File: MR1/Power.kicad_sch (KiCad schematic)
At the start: 39 parts, among them J3 USB_C_Receptacle_USB2.0, U1 LM27762, U11 LP5907MFX-1.8, U33 NCP163ASN330T1G, U4 LT3045xDD, U5 LT3094xDD, U7 SN65220

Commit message: Signed-off-by: lokimetasmith <lokimail@gmail.com>
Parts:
- removed C34: 100nF, Capacitor_SMD:C_0402_1005Metric, symbol Device:C
- removed U11: LP5907MFX-1.8, Package_TO_SOT_SMD:SOT-23-5, symbol Regulator_Linear:LP5907MFX-1.8
- added C40, C42: 100u, symbol Device:C_Polarized_Small_US
- added D1, D2: 1N4148WS, Diode_SMD:D_SOD-323, symbol Diode:1N4148WS
- added Q1: BCP53, Package_TO_SOT_SMD:SOT-223-3_TabPin2, symbol Transistor_BJT:BCP53
- added Q2: BCP56, Package_TO_SOT_SMD:SOT-223-3_TabPin2, symbol Transistor_BJT:BCP56
- added R49, R50: 1K, Resistor_SMD:R_0402_1005Metric, symbol Device:R
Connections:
- net +Vp: now also D1.2 (A), Q2.3 (E); no longer C15.2, R24.2, U1.11 (OUT+)
- net -Vp: now also D2.1 (K), Q1.3 (E); no longer C14.1, R18.1, U1.6 (OUT-), U5.1 (IN), U5.13 (IN), U5.2 (IN), U5.3 (EN/UV)
- net GND: now also C14.2, C15.1, C16.2, C18.2, R25.1, R26.2, U1.13 (PAD), U1.4 (GND), C40.2, C42.1
- net GNDA: no longer C14.2, C15.1, C16.2, C18.2, R25.1, R26.2, U1.13 (PAD), U1.4 (GND)
- new net: C42.2, D2.2 (A), Q1.1 (B), R50.2
- new net: C40.1, D1.1 (K), Q2.1 (B), R49.2
- new net: U5.1 (IN), U5.13 (IN), U5.2 (IN), U5.3 (EN/UV)
- new net +Vp_cm: C15.2, Q2.2 (C), Q2.4 (C), R24.2, R49.1, U1.11 (OUT+)
- new net -Vp_cm: C14.1, Q1.2 (C), Q1.4 (C), R18.1, R50.1, U1.6 (OUT-)
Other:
- moved on the sheet: C10, C118, C121, C17, D82, R145, U33

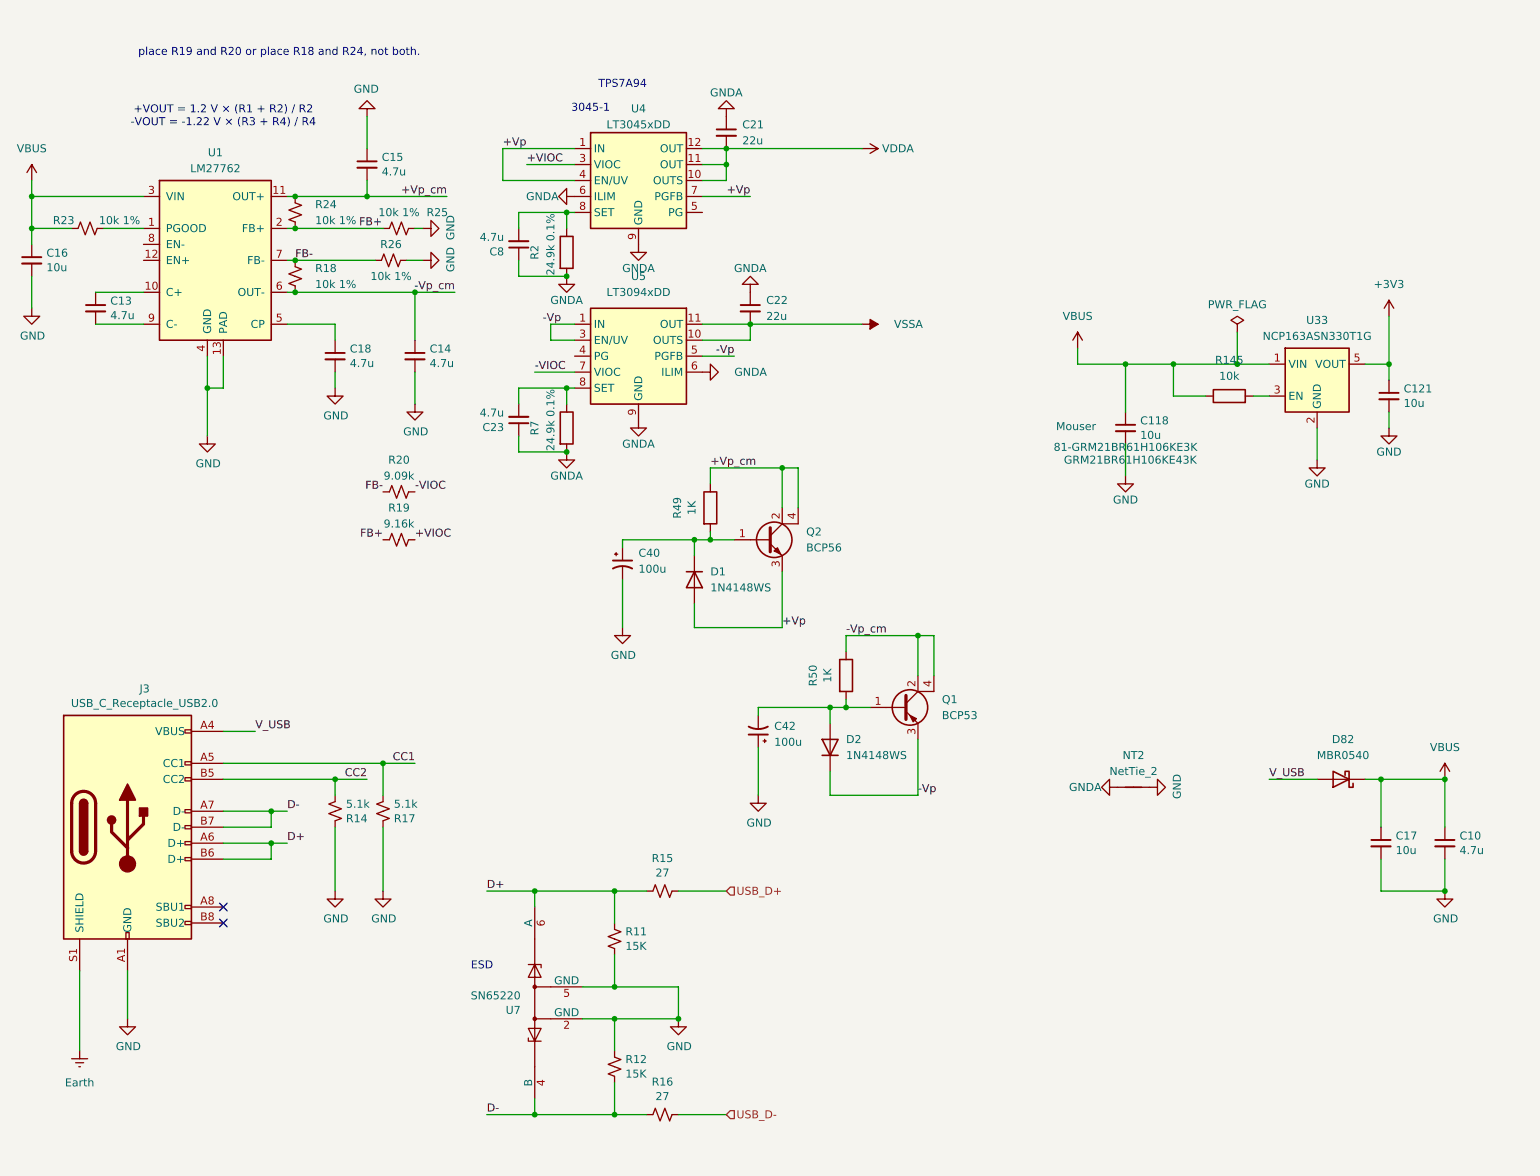
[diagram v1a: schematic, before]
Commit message: feat(cad,firmware,interposer): PTFE interposer, deliverables pipeline, and firmware
- CAD & Interposer:
  - Modeled PTFE_Interposer (55.0 x 51.962 x 0.8 mm) with central wafer diamond cutout
  - Dual-sided silver chloride (Ag/AgCl) ribbon electrode pads (30 deg Cis, 210 deg Trans)
  - 6-pad pogo pin landing array and 4 fluidic pass-throughs with weep duct relief
  - Verified 0 physical collisions across cartridge stack and housings (100% green)
- Deliverables & Export Pipeline:
  - Created automated export system (Makefile, scripts/export_manager.py, scripts/export_all.sh)
  - Full cataloging of 159 deliverables (30 STLs, 13 DXFs, STEPs, Gerbers, WireViz)
  - Added E2E tests (tests/test_exports_e2e.py) and legacy parity tests (tests/test_legacy_feature_parity.py)
- Firmware & Schematics:
  - ESP32-S3 firmware with 100 kHz USB streaming, FreeRTOS dual-core tasks, Web UI
  - Added fast AD40xx SPI driver, MCP4822 DAC driver, leak detection, and pump UART
  - SBU auto-polarity detection and I2C routing in MR1 schematics
- Docs & Environment:
  - Added setup_env.sh, setup_env.ps1, requirements.txt, EXPORTS.md
  - Updated README.md, TODO.md, atlas.project.json, and walkthrough.md
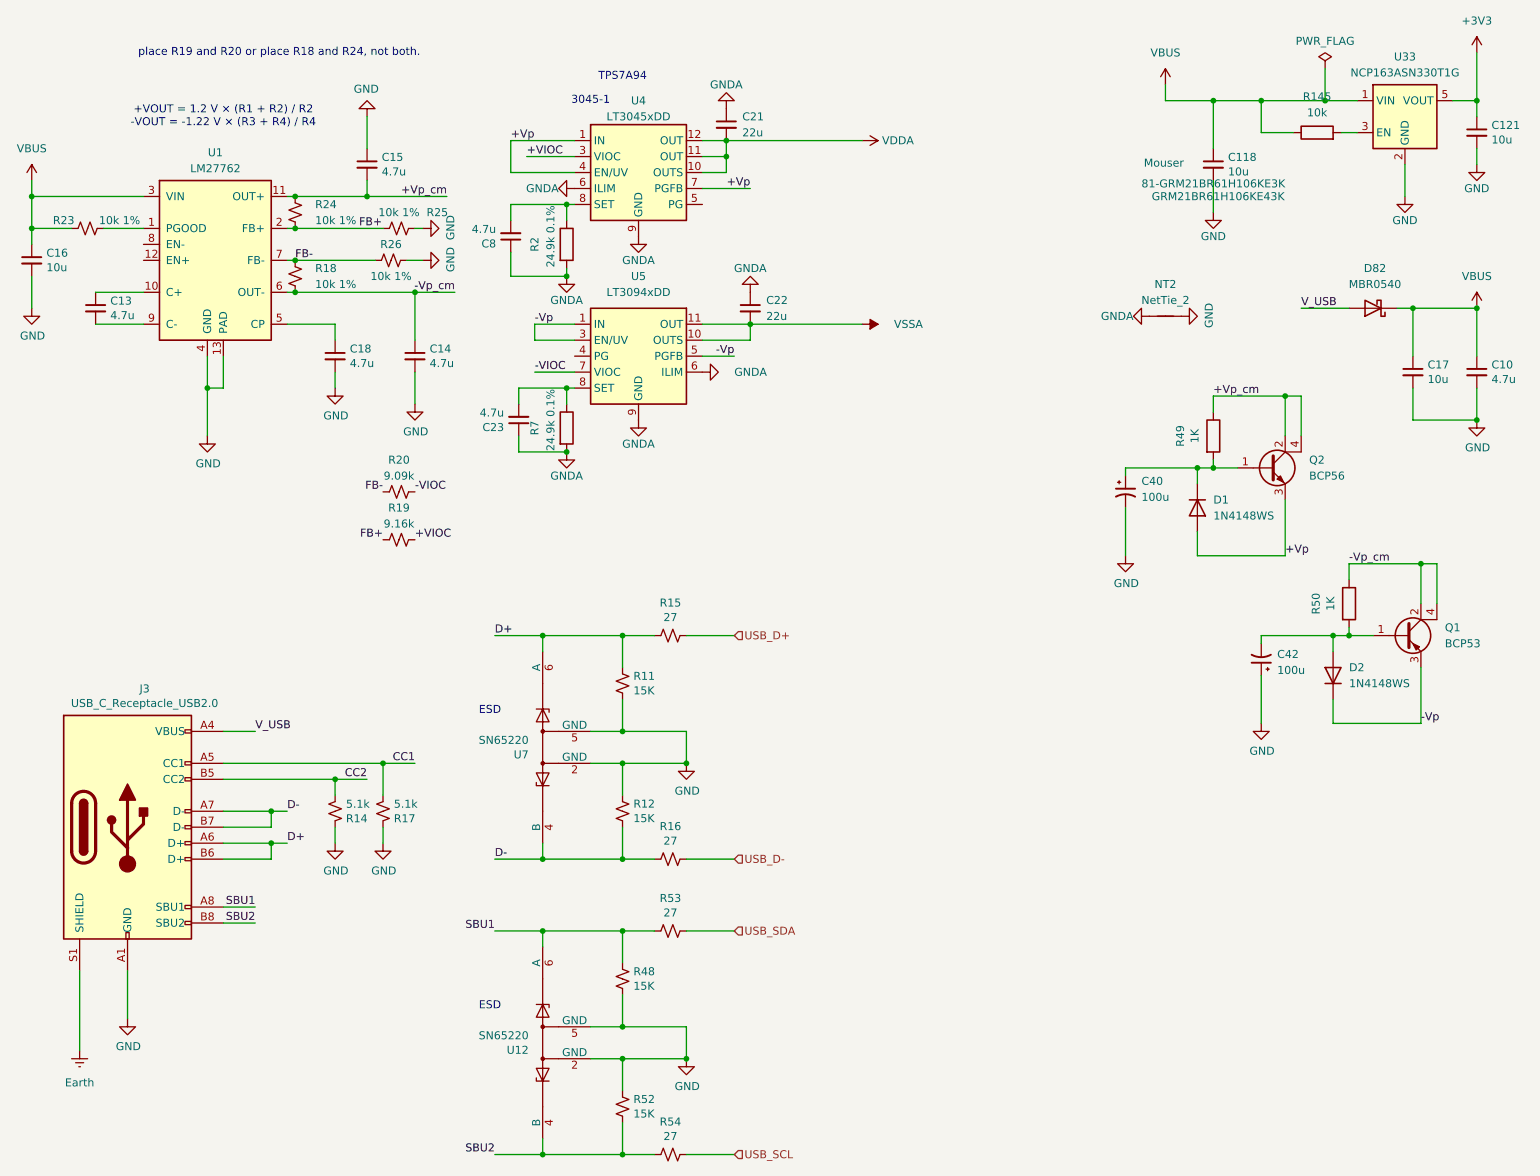
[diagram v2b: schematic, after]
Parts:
- added R48, R52: 15K, Resistor_SMD:R_0402_1005Metric, symbol temp-sensor-rescue:R_Small_US-Device-temp-sensor-rescue
- added R53, R54: 27, Resistor_SMD:R_0402_1005Metric, symbol temp-sensor-rescue:R_Small_US-Device-temp-sensor-rescue
- added U12: SN65220, Package_TO_SOT_SMD:SOT-23-6, symbol twig:SN65220-Power_Protection_passthrough
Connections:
- net -Vp: now also U5.1 (IN), U5.13 (IN), U5.2 (IN), U5.3 (EN/UV)
- net GND: now also R48.2, R52.1, U12.2 (GND), U12.5 (GND)
- net SBU1: now reaches J3.A8 (SBU1)
- net SBU1: now also R48.1, R53.1, U12.1, U12.6 (A)
- net SBU2: now reaches J3.B8 (SBU2)
- net SBU2: now also R52.2, R54.1, U12.3, U12.4 (B)
- new net USB_SCL: R54.2
- new net USB_SDA: R53.2
- no-connect marks 2 -> 0
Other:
- moved on the sheet: C10, C118, C121, C17, C21, C40, C42, C8, D1, D2, D82, NT2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

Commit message: commiting pcb changes
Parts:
- Q1: value BCP53 -> 2SA1037; footprint Package_TO_SOT_SMD:SOT-223-3_TabPin2 -> Package_TO_SOT_SMD:SOT-23; symbol Transistor_BJT:BCP53 -> Transistor_BJT:Q_PNP_BEC
- Q2: value BCP56 -> CMBT2222A; footprint Package_TO_SOT_SMD:SOT-223-3_TabPin2 -> Package_TO_SOT_SMD:SOT-23; symbol Transistor_BJT:BCP56 -> Transistor_BJT:Q_NPN_BEC
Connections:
- net +Vp: now also Q2.2 (E); no longer Q2.3 (E)
- net +Vp_cm: now also Q2.3 (C); no longer Q2.2 (C), Q2.4 (C)
- net -Vp: now also Q1.2 (E); no longer Q1.3 (E)
- net -Vp_cm: now also Q1.3 (C); no longer Q1.2 (C), Q1.4 (C)
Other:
- moved on the sheet: C40, D1, R49

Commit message: updated board, and worked to improve the project, added .agents which might be a mistake, along with the board updates
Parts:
- C40, C42: footprint (none) -> Capacitor_SMD:C_1206_3216Metric; symbol Device:C_Polarized_Small_US -> Device:C
- U4: footprint Package_DFN_QFN:DFN-12-1EP_3x3mm_P0.5mm_EP1.6x2.5mm -> Package_DFN_QFN:DFN-12-1EP_3x3mm_P0.45mm_EP1.65x2.38mm_ThermalVias
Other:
- moved on the sheet: C21, C22, C23, C8, R2, R7, U4, U5
